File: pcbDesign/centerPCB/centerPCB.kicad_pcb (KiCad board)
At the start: 4 copper layers, 157 x 58.8 mm, 11 parts, among them J1 Conn_01x07_Pin, J2 Conn_01x12_Pin

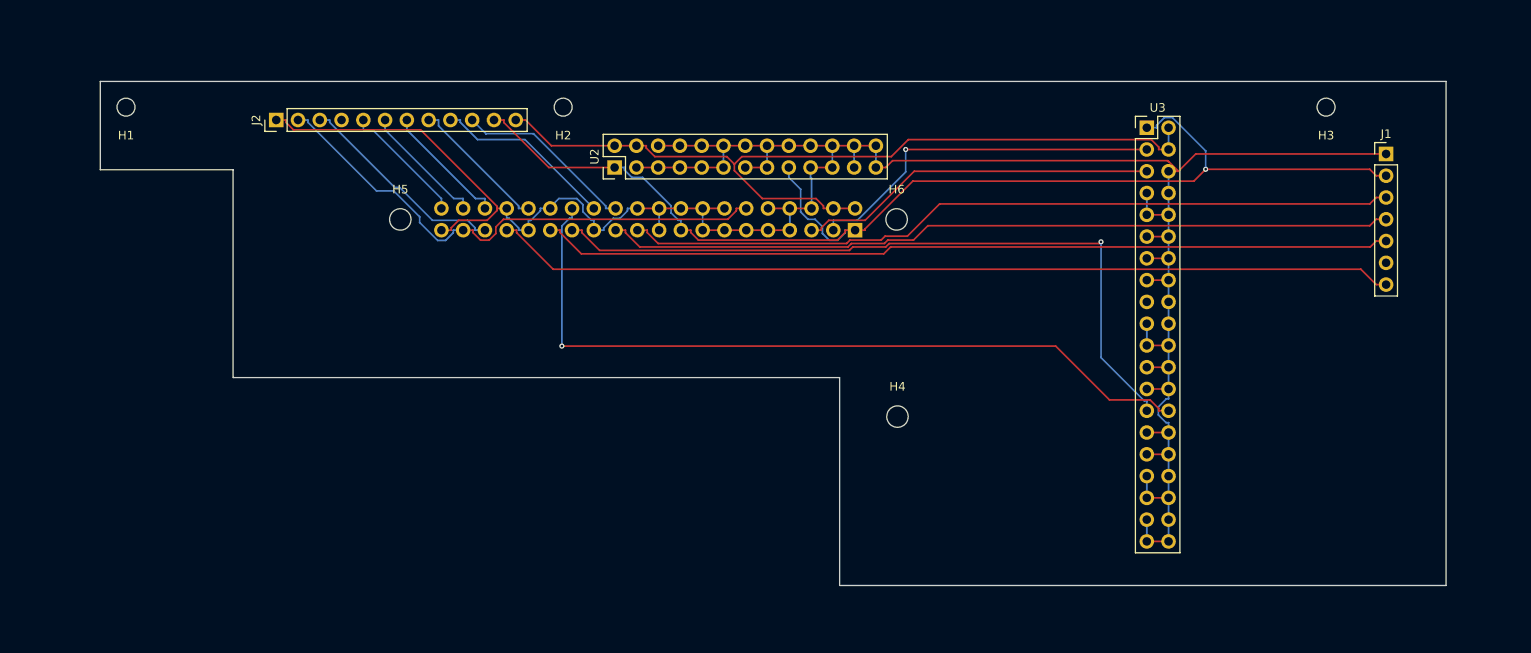
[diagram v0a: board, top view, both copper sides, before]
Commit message: Finalized center and left pcbs placemnt
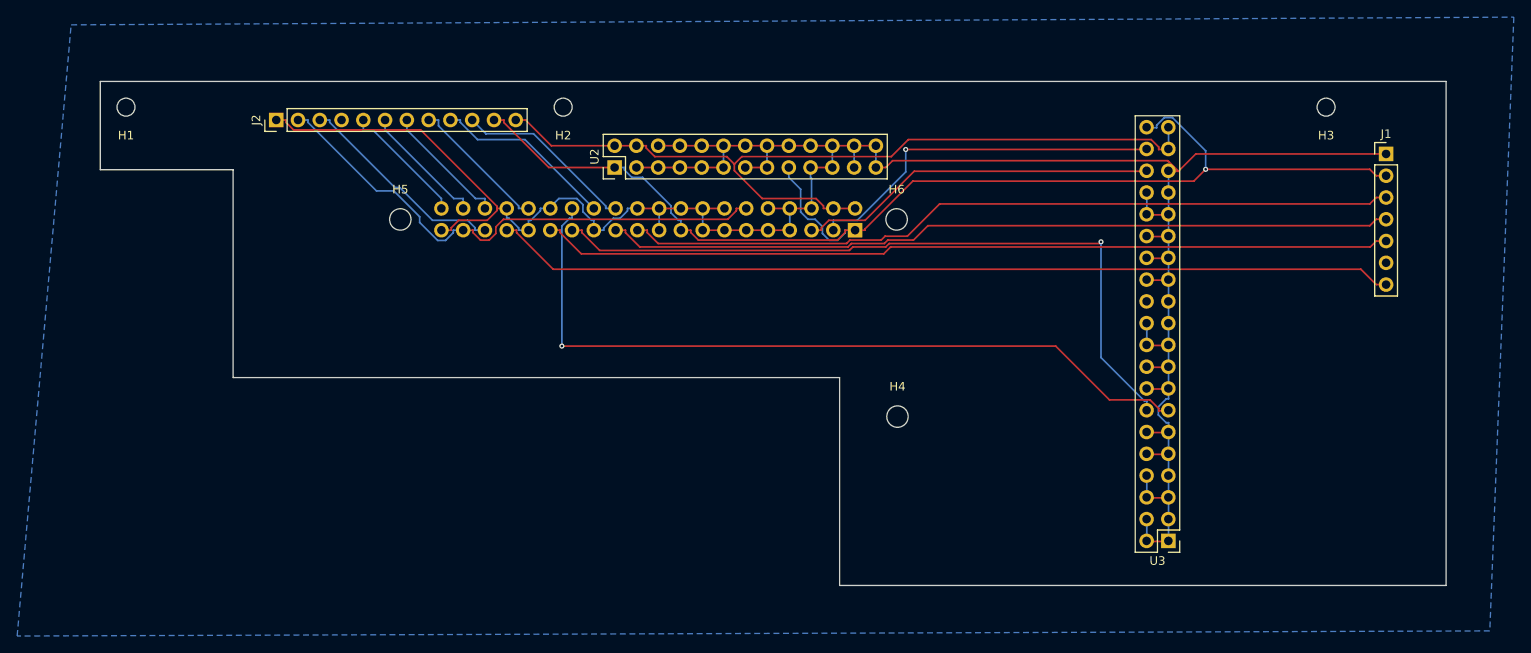
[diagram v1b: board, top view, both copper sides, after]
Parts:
- moved U3 48.3 mm to (182.6, 106.3), turned to 180 degrees
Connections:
- J2 pad 11: /3v3 -> /Clk
- U1 pad 10: GND -> /Volume_A
- U1 pad 12: /Volume_B -> /Clk
- U1 pad 8: GND -> /Brightness_B
- U2 pad 1: /3v3 -> GND
- U2 pad 17: /3v3 -> GND
- U3 pad 17: unconnected-(U3-3V3-Pad17) -> /3v3
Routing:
- net GND: track 299.2 -> 289.0 mm
- net /3v3: track 141.4 -> 146.5 mm
- net /MCU SCL: track 42.1 -> 44.7 mm
- net /EEPROM SDA: track 85.4 -> 87.9 mm
- net /MCU SDA: track 42.7 -> 45.2 mm
- net /5v: track 99.7 -> 97.1 mm
- added copper zone on B.Cu, net GND
- removed copper zone on In1.Cu, net GND
- removed copper zone on In2.Cu, net GND
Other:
- copper layers 4 -> 2

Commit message: rerouted
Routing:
- net /Brightness_B: track 0.00 -> 86.5 mm, vias 0 -> 1
- net /Volume_A: track 0.00 -> 55.3 mm
- net /Volume_B: track 62.1 -> 24.9 mm
- net /Clk: track 0.00 -> 36.5 mm, vias 0 -> 2
- net /MCU SDA: track 45.2 -> 70.2 mm
- net /MCU SCL: track 44.7 -> 69.2 mm, vias 0 -> 1
- net /5v: track 97.1 -> 119.7 mm, vias 0 -> 2
- net /EEPROM SDL: track 90.8 -> 70.0 mm, vias 1 -> 0
- net GND: track 289.0 -> 308.1 mm
- net /3v3: track 146.5 -> 137.4 mm, vias 1 -> 2
- net /Power_LED: track 21.2 -> 29.5 mm, vias 0 -> 1
- net /EEPROM SDA: track 87.9 -> 82.3 mm
- net /LR_Clk: track 24.9 -> 27.6 mm
- net /1: track 99.4 -> 100.8 mm
- net /Start: track 90.4 -> 89.1 mm
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
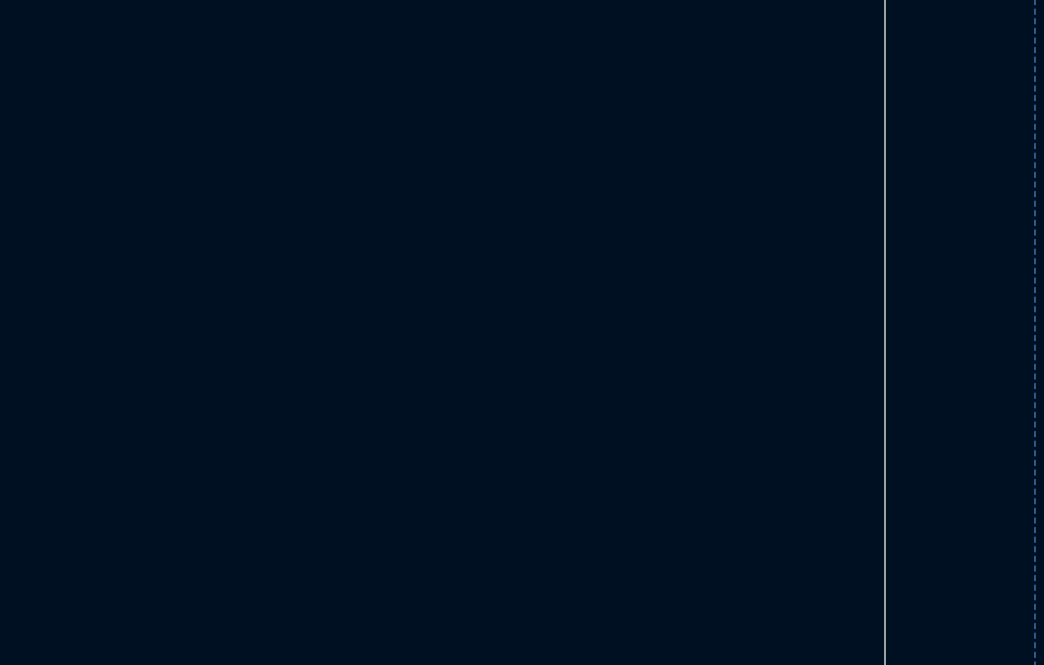
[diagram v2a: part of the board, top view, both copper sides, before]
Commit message: Added names on silk layer
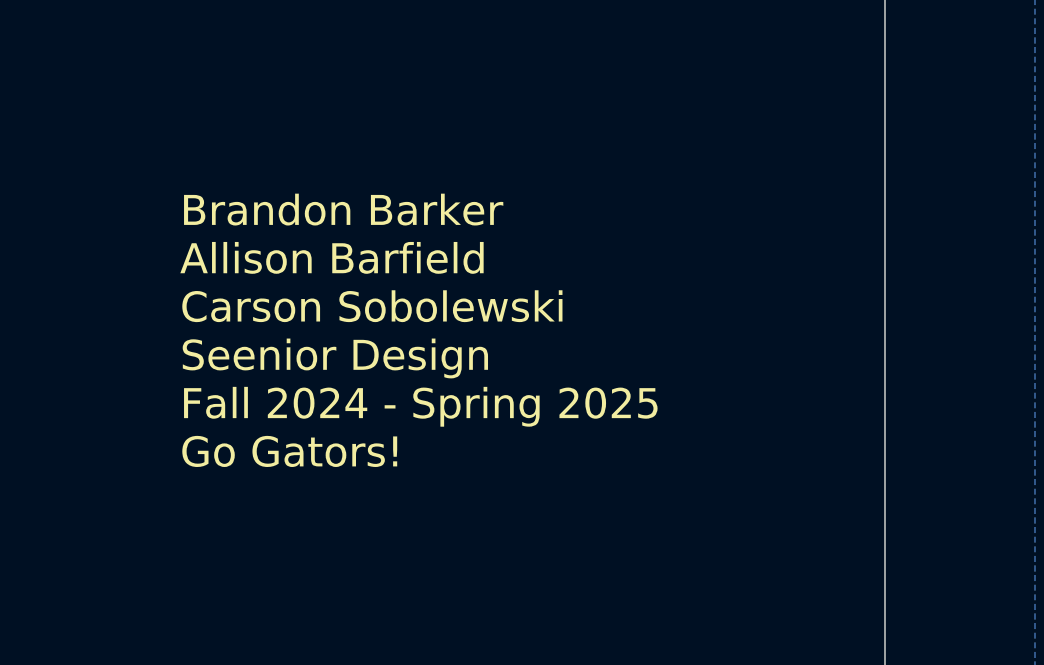
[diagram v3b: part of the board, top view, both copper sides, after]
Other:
- board text added: "Brandon Barker Allison Barfield Carson Sobolewski Seenior Design Fall 2024 - Spring 2025 Go Gators!"
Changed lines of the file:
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@@
 		(layer "Edge.Cuts")
+	)
+	(gr_text "Brandon Barker\nAllison Barfield\nCarson Sobolewski\nSeenior Design\nFall 2024 - Spring 2025\nGo Gators!"
+		(at 191.5 102.5 0)
+		(layer "F.SilkS")
+		(effects
+			(font
+				(size 1 1)
+				(thickness 0.1)
+			)
+			(justify left bottom)
+		)
 	)
 	(segment

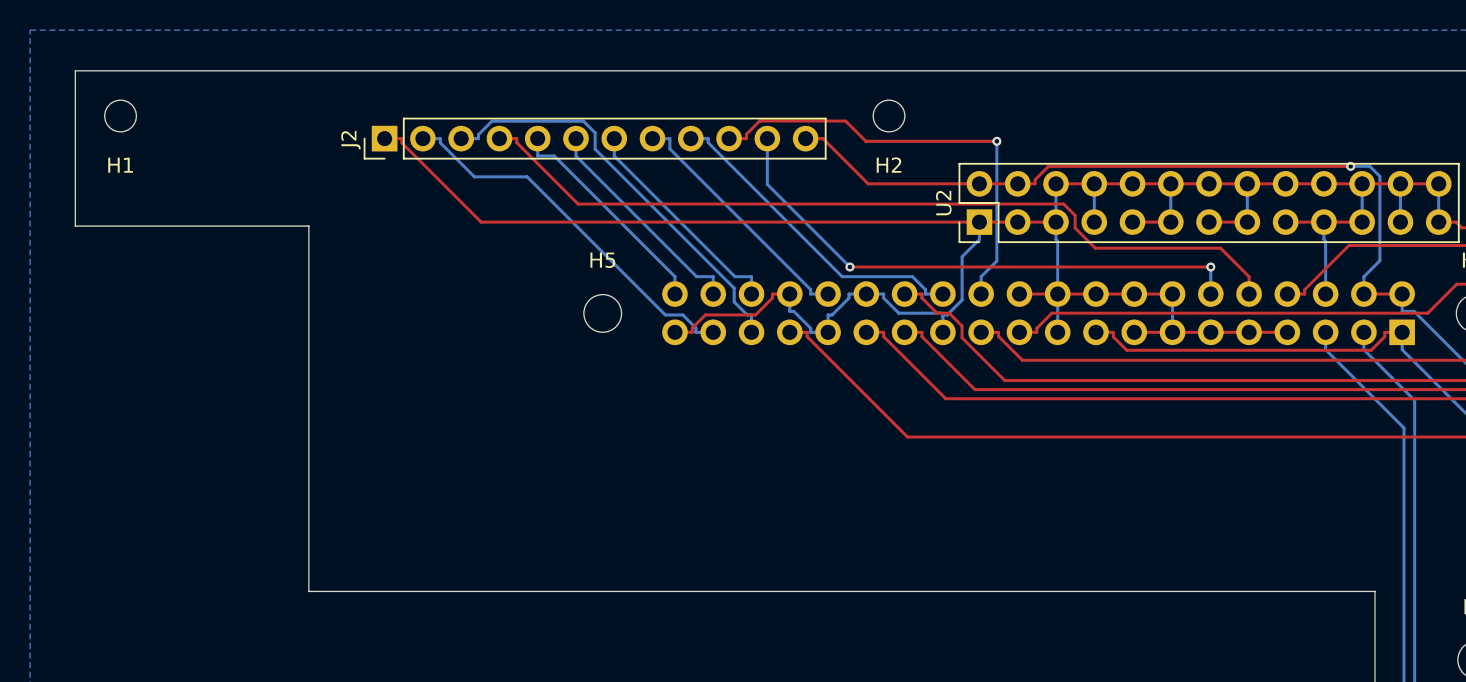
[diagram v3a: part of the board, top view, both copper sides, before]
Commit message: Fixed overlapping boards issues by cutting out areas in design Rerouted dpad traces to not interfere with each other Added "filesForOrder"
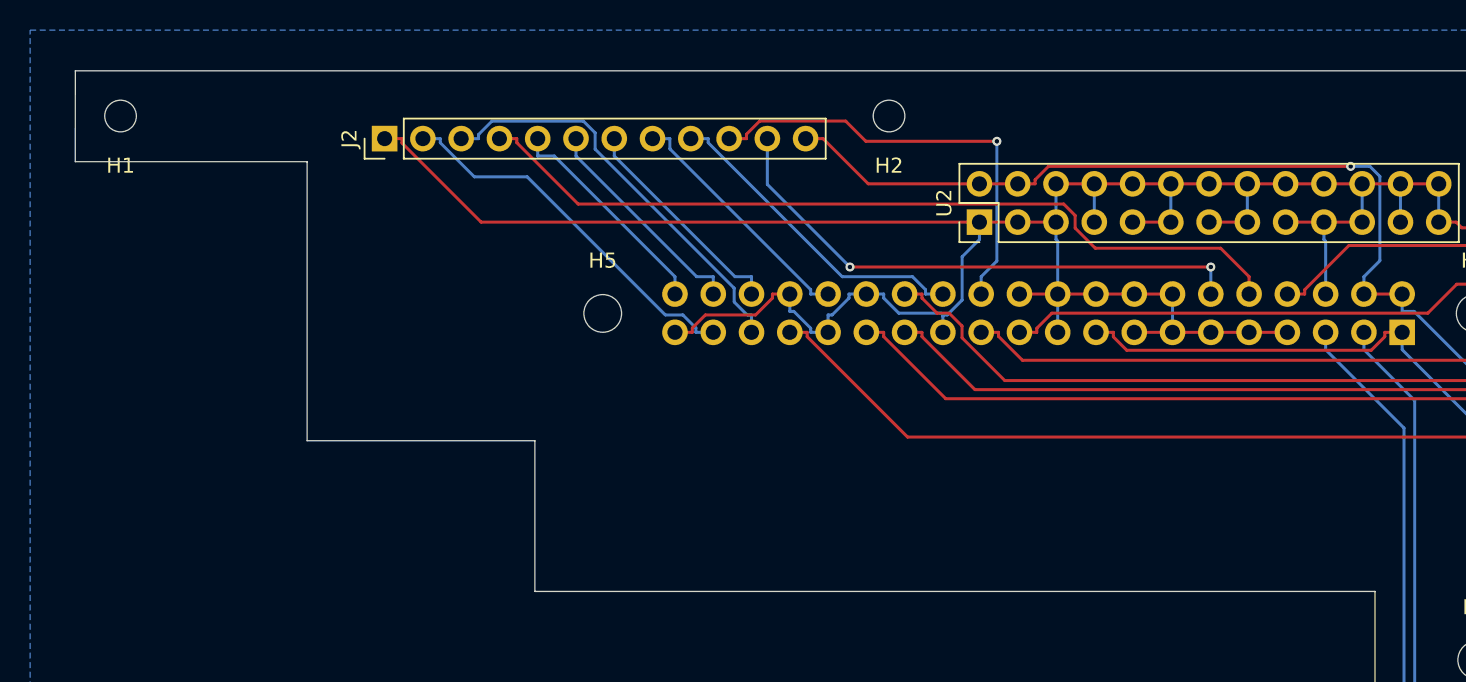
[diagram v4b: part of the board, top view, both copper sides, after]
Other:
- outline, holes or cut-outs redrawn
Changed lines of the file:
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@@
 	)
 	(gr_line
-		(start 73.5 87.25)
+		(start 88.5 87.25)
 		(end 144.250111 87.25)
 		(stroke
 			(width 0.05)
-			(type default)
+			(type solid)
 		)
 		(layer "Edge.Cuts")
@@
 	)
 	(gr_line
-		(start 73.5 63)
-		(end 73.5 87.25)
+		(start 73.38 58.73)
+		(end 73.38 77.25)
 		(stroke
 			(width 0.05)
-			(type default)
+			(type solid)
+		)
+		(layer "Edge.Cuts")
+	)
+	(gr_line
+		(start 88.5 77.25)
+		(end 73.38 77.25)
+		(stroke
+			(width 0.05)
+			(type solid)
 		)
 		(layer "Edge.Cuts")
@@
 	(gr_line
 		(start 57.9999 52.7002)
-		(end 57.9999 63)
+		(end 57.994975 58.73)
 		(stroke
 			(width 0.05)
@@
 	)
 	(gr_line
-		(start 57.9999 63)
-		(end 73.5 63)
+		(start 88.5 87.25)
+		(end 88.5 77.25)
 		(stroke
 			(width 0.05)
+			(type solid)
+		)
+		(layer "Edge.Cuts")
+	)
+	(gr_line
+		(start 57.994975 58.73)
+		(end 73.405025 58.73)
+		(stroke
+			(width 0.05)
